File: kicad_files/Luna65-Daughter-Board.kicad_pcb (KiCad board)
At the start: 2 copper layers, 25.1 x 25.1 mm, 29 parts, among them J1 TYPE-C-31-M12_13, J2 Molex Power, J3 JSTPH, J4 Conn_01x03, U1 MCP73831, U2 USBLC6-2SC6, U3 AP2112

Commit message: DB Rev B
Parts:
- removed H2, H3: MountingHole, MountingHole:MountingHole_2.2mm_M2
- removed J4: Conn_01x03, Connector_PinHeader_1.27mm:PinHeader_1x03_P1.27mm_Vertical
- added C10: 22uF, acheron_Components:C_0805_2012Metric, F.Cu at (83.5, 37.6)
- added C8: 10uF, acheron_Components:C_0805_2012Metric, F.Cu at (79.1, 32.7)
- added C9: 1uF, acheron_Components:C_0805_2012Metric, F.Cu at (80.0, 39.1)
- added D4: MBR120, acheron_Components:D_SOD-123, F.Cu at (62.6, 41.1)
- added L1: LPS3015-222ML, Luna65:LPS3015, F.Cu at (83.6, 34.7)
- added R10: 3.6M, Resistor_SMD:R_0805_2012Metric, F.Cu at (76.3, 33.6)
- added R11: 261K, Resistor_SMD:R_0805_2012Metric, F.Cu at (76.3, 37.1)
- added U4: TPS61202DRC, Package_SON:Texas_S-PVSON-N10_ThermalVias, F.Cu at (79.6, 36.0)
- R1, R2, R3, R4, R5, R6, R7, R8, R9: footprint Resistor_SMD:R_0805_2012Metric_Pad1.20x1.40mm_HandSolder -> Resistor_SMD:R_0805_2012Metric
- moved R4 23.0 mm to (63.7, 29.4), turned to 180 degrees
- moved H1 21.3 mm to (63.4, 23.6)
- moved U1 19.8 mm to (63.4, 32.2)
- moved R6 18.1 mm to (63.7, 27.4), turned to 0 degrees
- moved H4 18.0 mm to (83.1, 23.6)
- moved C5 16.7 mm to (82.7, 27.8), turned to 0 degrees
- moved R9 16.2 mm to (82.7, 29.8), turned to 180 degrees
- moved C2 16.1 mm to (63.7, 34.9), turned to 180 degrees
- moved D1 14.9 mm to (66.6, 23.6)
- moved D2 14.7 mm to (83.9, 41.1)
- moved D3 11.5 mm to (79.7, 23.6)
- moved J3 10.3 mm to (68.9, 42.6)
- moved J2 7.62 mm to (78.0, 43.1)
- moved C1 6.28 mm to (79.1, 30.8), turned to 180 degrees
- moved R1 5.06 mm to (79.1, 28.8), turned to 0 degrees
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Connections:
- C3 pad 2: VBUS -> VUSB
- C4 pad 1: VBUS -> 5V
- D1 pad 2: VBUS -> VUSB
- D2 pad 1: VBUS -> 5V
- D2 pad 2: VBAT -> Net-(C10-Pad1)
- J1 pad A4: VBUS -> VUSB
- J1 pad B4: VBUS -> VUSB
- J2 pad 1: 3.3V -> D-
- J2 pad 2: VBUS -> D+
- J2 pad 3: D- -> 3.3V
- J2 pad 4: D+ -> 5V
- R8 pad 1: VBUS -> 5V
- U1 pad 4: VBUS -> VUSB
- U2 pad 5: VBUS -> VUSB
- U3 pad 1: VBUS -> 5V
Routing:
- net VUSB: track 0.00 -> 47.2 mm, vias 0 -> 7
- net VBAT: track 19.3 -> 37.6 mm, vias 2 -> 3
- net GND: track 3.95 -> 20.3 mm, vias 0 -> 2
- net VBUS: track 13.6 -> 0.00 mm, vias 9 -> 0
- net 3.3V: track 24.6 -> 15.3 mm, vias 1 -> 0
- net /SHIELD: track 12.2 -> 4.77 mm
- net Net-(C10-Pad1): track 0.00 -> 7.22 mm, vias 0 -> 2
- net Net-(R10-Pad2): track 0.00 -> 3.79 mm
- net Net-(R6-Pad1): track 1.90 -> 4.93 mm
- net Net-(C5-Pad1): track 4.24 -> 5.40 mm
- net 5V: track 0.00 -> 1.14 mm, vias 0 -> 5
- net D-: track 6.64 -> 7.44 mm
- net DBus+: track 5.91 -> 5.29 mm
- added copper zone on B.Cu, net 5V
- added copper zone on F.Cu, net 5V
- added copper zone on F.Cu, net Net-(C10-Pad1)
- added copper zone on F.Cu, net Net-(C9-Pad1)
- added copper zone on F.Cu, net Net-(L1-Pad2)
- added copper zone on F.Cu, net VBAT
- removed copper zone on B.Cu, net VBUS
- removed copper zone on F.Cu, net VBUS
- removed copper zone on F.Cu, net unconnected-(U3-Pad4)

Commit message: DB Rev C
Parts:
- removed the C9 at (80.0, 39.1)
- removed D4: MBR120, acheron_Components:D_SOD-123
- removed H4: MountingHole, MountingHole:MountingHole_2.2mm_M2_Pad
- added C10: 220uF, Capacitor_SMD:C_1206_3216Metric, F.Cu at (113.5, 70.7)
- added C7: 0.1uF, acheron_Components:C_0805_2012Metric, F.Cu at (109.3, 60.1)
- added H2: MountingHole, MountingHole:MountingHole_2.2mm_M2_Pad, F.Cu at (112.6, 52.7)
- added Q1: MMUN2133LT1G, Package_TO_SOT_SMD:SOT-23, F.Cu at (99.1, 63.3)
- added R12: 100K, Resistor_SMD:R_0805_2012Metric, F.Cu at (109.3, 62.1)
- added R13: 1K, Resistor_SMD:R_0805_2012Metric, F.Cu at (92.3, 66.0)
- added U5: TPS61032RSAR, Package_DFN_QFN:Texas_S-PVQFN-N16_EP2.7x2.7mm, F.Cu at (110.3, 65.7)
- C9: renamed from C10; value 22uF -> 2.2uF
- D2: value MBR120 -> Red; footprint acheron_Components:D_SOD-123 -> LED_SMD:LED_1206_3216Metric_Pad1.42x1.75mm_HandSolder
- J1: value TYPE-C-31-M12_13 -> TYPE-C-31-M12
- L1: value LPS3015-222ML -> 6.8uH XAL4030; footprint Luna65:LPS3015 -> Luna65:XAL4030
- R10: value 3.6M -> 2.34M
- R11: value 261K -> 390K
- R4: value 10K -> 1K
- U4: value TPS61202DRC -> APX803L; footprint Package_SON:Texas_S-PVSON-N10_ThermalVias -> Package_TO_SOT_SMD:SOT-23
- moved R7 42.2 mm to (104.7, 59.4)
- moved R2 42.1 mm to (106.6, 59.4)
- moved R4 41.8 mm to (95.9, 56.1), turned to 0 degrees
- moved D1 41.5 mm to (96.3, 52.7)
- moved C5 41.5 mm to (113.1, 56.1)
- moved C3 41.5 mm to (102.8, 59.4), turned to -90 degrees
- moved D3 41.5 mm to (109.3, 52.6)
- moved R9 41.5 mm to (113.1, 58.0)
- moved H1 41.5 mm to (93.0, 52.7)
- moved J1 41.5 mm to (102.8, 56.8)
- moved C9 41.4 mm to (113.9, 65.8), turned to 90 degrees
- moved J3 41.4 mm to (98.4, 71.6)
- moved J2 41.3 mm to (107.5, 72.0)
- moved U2 41.3 mm to (102.5, 63.2)
- moved R10 41.1 mm to (105.9, 62.1), turned to 0 degrees
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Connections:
- C9 pad 1: Net-(C10-Pad1) -> 5V
- D2 pad 1: 5V -> GND
- D2 pad 2: Net-(C10-Pad1) -> Net-(D2-Pad2)
- J2 pad 1: D- -> 3.3V
- J2 pad 2: D+ -> 5V
- J2 pad 3: 3.3V -> D-
- J2 pad 4: 5V -> D+
- J3 pad NC1: (no net) -> GND
- J3 pad NC2: (no net) -> GND
- U4 pad 1: Net-(C9-Pad1) -> GND
- U4 pad 2: Net-(C10-Pad1) -> /EN
- U4 pad 3: Net-(L1-Pad2) -> VBAT
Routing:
- net VUSB: track 47.2 -> 4.45 mm, vias 7 -> 5
- net VBAT: track 37.6 -> 2.50 mm, vias 3 -> 11
- net 3.3V: track 15.3 -> 0.00 mm
- net /LBO: track 0.00 -> 11.8 mm, vias 0 -> 2
- net /EN: track 0.00 -> 7.52 mm, vias 0 -> 2
- net Net-(C10-Pad1): track 7.22 -> 0.00 mm, vias 2 -> 0
- net Net-(Q1-Pad3): track 0.00 -> 6.62 mm, vias 0 -> 2
- net GND: track 20.3 -> 15.1 mm, vias 2 -> 10
- net Net-(D2-Pad2): track 0.00 -> 3.52 mm
- net Net-(J1-PadB5): track 2.95 -> 6.46 mm, vias 0 -> 2
- net Net-(R6-Pad1): track 4.93 -> 1.82 mm
- net Net-(R4-Pad1): track 1.87 -> 4.84 mm
- net Net-(J1-PadA5): track 3.23 -> 6.16 mm, vias 0 -> 2
- net Net-(D1-Pad1): track 3.17 -> 5.68 mm, vias 0 -> 2
- net D+: track 7.15 -> 8.84 mm, vias 0 -> 2
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- added copper zone on B.Cu, net GND
- added copper zone on B.Cu, net VBAT
- added copper zone on B.Cu, net VUSB
- removed copper zone on B.Cu, net 5V
- removed copper zone on F.Cu, net Net-(C10-Pad1)
- removed copper zone on F.Cu, net Net-(C9-Pad1)
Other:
- rule pad_to_mask_clearance: 0 -> 0.0508

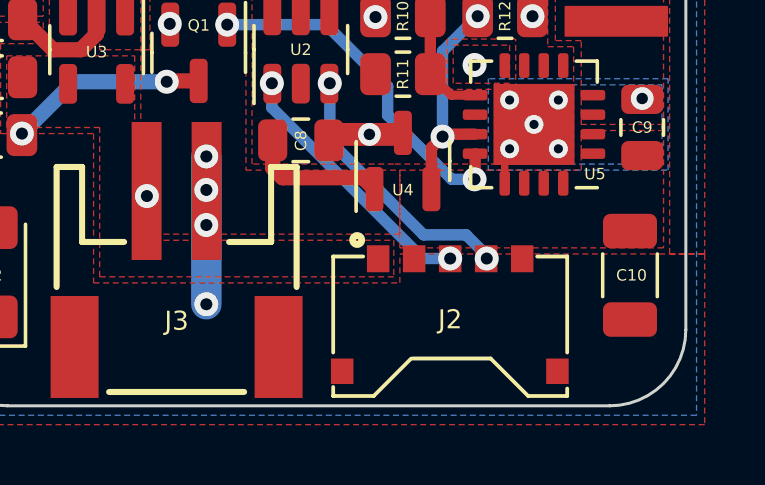
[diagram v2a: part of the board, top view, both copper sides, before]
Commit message: Updated QMK firmware to support RGB. Cleaned up routing somewhat
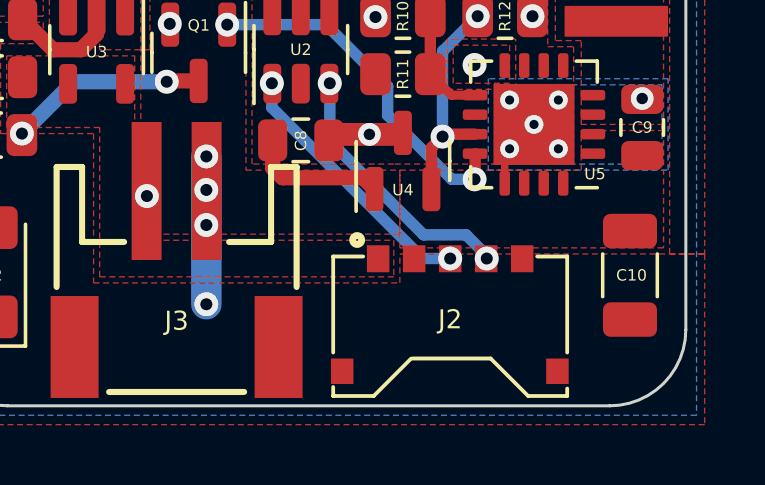
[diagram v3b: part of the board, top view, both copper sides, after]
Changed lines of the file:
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@@
     (pad "2" smd roundrect (at 1.4875 0 90) (size 1.425 1.75) (layers "F.Cu" "F.Paste" "F.Mask") (roundrect_rratio 0.1754392982)
       (net 4 "VUSB") (pinfunction "A") (pintype "passive"))
-    (model "${KICAD6_3DMODEL_DIR}/LED_SMD.3dshapes/LED_1206_3216Metric.wrl"
+    (model "${KICAD6_3DMODEL_DIR}/LED_SMD.3dshapes/LED_1206_3216Metric.step"
       (offset (xyz 0 0 0))
       (scale (xyz 1 1 1))
@@
   )
   (footprint "Luna65:MOLEX_78171-0005" (layer "F.Cu")
-    (at 107.5182 72.011752)
+    (at 107.5182 72.011743)
     (property "Sheetfile" "Luna65-Daughter-Board.kicad_sch")
     (property "Sheetname" "")
@@
     (pad "P$6" smd rect locked (at -3.6 1.875) (size 0.75 0.85) (layers "F.Cu" "F.Paste" "F.Mask"))
     (pad "P$7" smd rect locked (at 3.575 1.875) (size 0.75 0.85) (layers "F.Cu" "F.Paste" "F.Mask"))
+    (model "${KIPRJMOD}/libraries/781710005.stp"
+      (offset (xyz 0 0 1.27))
+      (scale (xyz 1 1 1))
+      (rotate (xyz -90 0 0))
+    )
   )
   (footprint "Resistor_SMD:R_0805_2012Metric" (layer "F.Cu")
@@
     (pad "2" smd roundrect (at 1.65 0 90) (size 1 1.2) (layers "F.Cu" "F.Paste" "F.Mask") (roundrect_rratio 0.25)
       (net 5 "CASE") (pinfunction "A") (pintype "passive"))
-    (model "${KISYS3DMOD}/Diode_SMD.3dshapes/D_SOD-123.wrl"
+    (model "${KISYS3DMOD}/Diode_SMD.3dshapes/D_SOD-123.step"
       (offset (xyz 0 0 0))
       (scale (xyz 1 1 1))
@@
     (pad "NC2" smd rect (at 3.399993 -1.499997 270) (size 3.400001 1.6) (layers "F.Cu" "F.Paste" "F.Mask")
       (net 1 "GND") (solder_mask_margin 0.0508))
+    (model "${KIPRJMOD}/libraries/S2B-PH-SM4-TB.STEP"
+      (offset (xyz 0 3.175 0))
+      (scale (xyz 1 1 1))
+      (rotate (xyz -90 0 -180))
+    )
   )
   (footprint "Resistor_SMD:R_0805_2012Metric" (layer "F.Cu")
@@
     (pad "2" smd roundrect (at 1.4875 0 90) (size 1.425 1.75) (layers "F.Cu" "F.Paste" "F.Mask") (roundrect_rratio 0.1754392982)
       (net 26 "Net-(D2-Pad2)") (pinfunction "A") (pintype "passive"))
-    (model "${KICAD6_3DMODEL_DIR}/LED_SMD.3dshapes/LED_1206_3216Metric.wrl"
+    (model "${KICAD6_3DMODEL_DIR}/LED_SMD.3dshapes/LED_1206_3216Metric.step"
       (offset (xyz 0 0 0))
       (scale (xyz 1 1 1))
@@
     (pad "5" smd roundrect (at 1.1375 -0.95 270) (size 1.325 0.6) (layers "F.Cu" "F.Paste" "F.Mask") (roundrect_rratio 0.25)
       (net 13 "Net-(R4-Pad1)") (pinfunction "PROG") (pintype "input"))
-    (model "${KICAD6_3DMODEL_DIR}/Package_TO_SOT_SMD.3dshapes/SOT-23-5.wrl"
+    (model "${KICAD6_3DMODEL_DIR}/Package_TO_SOT_SMD.3dshapes/SOT-23-5.step"
       (offset (xyz 0 0 0))
       (scale (xyz 1 1 1))
@@
     (pad "17" smd rect (at 0 0 180) (size 2.7 2.7) (layers "F.Cu" "F.Mask")
       (net 1 "GND") (pinfunction "GND") (pintype "power_in"))
-    (model "${KICAD6_3DMODEL_DIR}/Package_DFN_QFN.3dshapes/Texas_S-PVQFN-N16_EP2.7x2.7mm.wrl"
-      (offset (xyz 0 0 0))
-      (scale (xyz 1 1 1))
+    (model "${KICAD6_3DMODEL_DIR}/Package_DFN_QFN.3dshapes/Texas_S-PVQFN-N16_EP2.7x2.7mm.step"
+      (offset (xyz 0 0 0))
+      (scale (xyz 1 1 1))

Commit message: Added 0 Ohm resistor to isolate BT and uC 3.3V
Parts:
- R2: value 5.1k -> 5.1K
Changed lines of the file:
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@@
       (effects (font (size 0.381 0.381) (thickness 0.0762)))
     )
-    (fp_text value "5.1k" (at 0 1.65 90) (layer "F.Fab")
+    (fp_text value "5.1K" (at 0 1.65 90) (layer "F.Fab")
       (effects (font (size 1 1) (thickness 0.15)))
     )
